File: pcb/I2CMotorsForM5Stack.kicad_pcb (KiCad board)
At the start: 2 copper layers, 60 x 50 mm, 33 parts, among them J1 FFC_connector, J2 2x15socket, J3 Conn_01x06, J4 Conn_01x06, U1 TB6612FNG, U2 ATmega328PB-MU

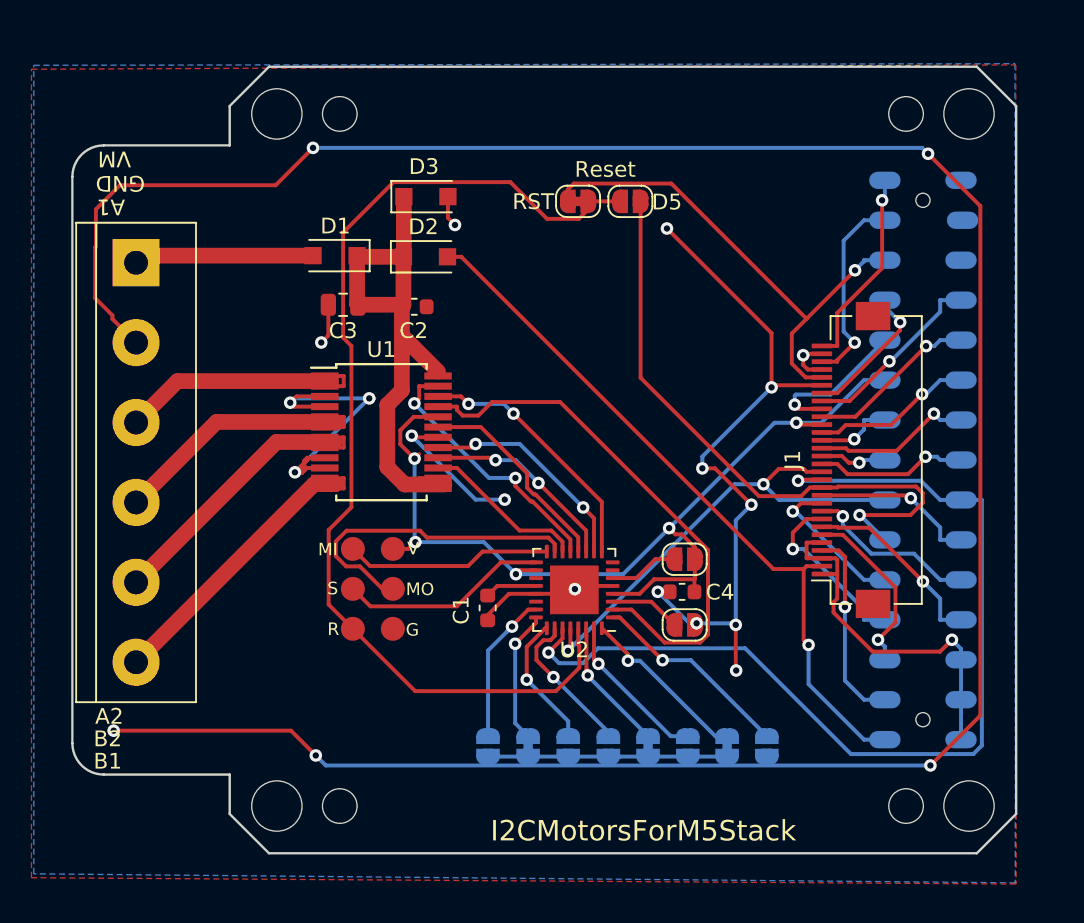
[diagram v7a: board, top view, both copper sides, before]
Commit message: Add connector to support power lines
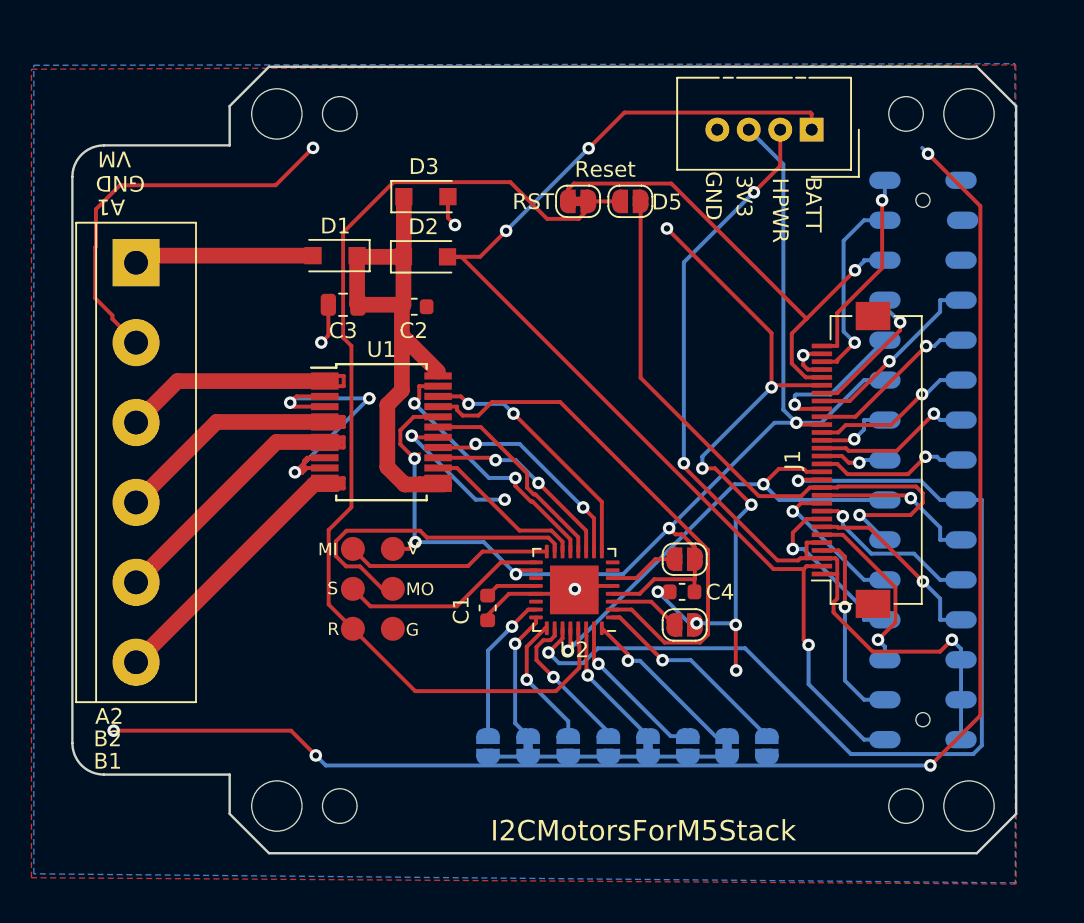
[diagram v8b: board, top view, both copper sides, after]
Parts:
- added J5: Conn_01x04, Connector:NS-Tech_Grove_1x04_P2mm_Vertical, F.Cu at (137.0, 54.0)
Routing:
- net GND: track 267.7 -> 229.0 mm
- net /HPWR: track 23.8 -> 58.1 mm, vias 1 -> 3
- net +BATT: track 45.9 -> 73.9 mm, vias 1 -> 3
- net +3V3: track 62.0 -> 81.9 mm
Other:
- board text added: "3V3"
- board text added: "BATT"
- board text added: "HPWR"
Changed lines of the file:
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@@
   (general
     (thickness 1.6)
-    (drawings 34)
-    (tracks 570)
+    (drawings 38)
+    (tracks 593)
     (zones 0)
-    (modules 33)
+    (modules 34)
     (nets 59)
   )
@@
     (add_net /VM)
     (add_net VCC)
+  )
+  (module Connector:NS-Tech_Grove_1x04_P2mm_Vertical (layer F.Cu)
+    (at 137 54 270)
+    (descr https://statics3.seeedstudio.com/images/opl/datasheet/3470130P1.pdf)
+    (tags Grove-1x04)
+    (fp_text reference J5 (at -1.5 -4 90) (layer F.SilkS) hide
+      (effects (font (size 1 1) (thickness 0.15)))
+    )
+    (fp_text value Conn_01x04 (at 4.19 2.83) (layer F.Fab)
+      (effects (font (size 1 1) (thickness 0.15)))
+    )
+    (fp_line (start -2.9 8.1) (end -2.9 -2.1) (layer F.Fab) (width 0.1))
+    (fp_line (start 2.2 8.1) (end -2.9 8.1) (layer F.Fab) (width 0.1))
+    (fp_line (start 2.2 -2.1) (end 2.2 8.1) (layer F.Fab) (width 0.1))
+    (fp_line (start -2.9 -2.1) (end 2.2 -2.1) (layer F.Fab) (width 0.1))
+    (fp_line (start -3.3 5.9) (end -3.3 8.55) (layer F.SilkS) (width 0.12))
+    (fp_line (start -3.3 -2.5) (end -3.3 0.15) (layer F.SilkS) (width 0.12))
+    (fp_line (start -3.3 8.55) (end 2.55 8.55) (layer F.SilkS) (width 0.12))
+    (fp_line (start -3.3 1.25) (end -3.3 4.75) (layer F.SilkS) (width 0.12))
+    (fp_line (start -3.3 -2.5) (end 2.55 -2.5) (layer F.SilkS) (width 0.12))
+    (fp_line (start 2.55 -2.5) (end 2.55 8.55) (layer F.SilkS) (width 0.12))
+    (fp_line (start -3.3 0.4) (end -3.3 1) (layer F.SilkS) (width 0.12))
+    (fp_line (start -3.3 5) (end -3.3 5.6) (layer F.SilkS) (width 0.12))
+    (fp_line (start -3.45 -2.65) (end 2.7 -2.65) (layer F.CrtYd) (width 0.05))
+    (fp_line (start 2.7 8.7) (end 2.7 -2.65) (layer F.CrtYd) (width 0.05))
+    (fp_line (start -3.45 8.7) (end 2.7 8.7) (layer F.CrtYd) (width 0.05))
+    (fp_line (start -3.45 -2.65) (end -3.45 8.7) (layer F.CrtYd) (width 0.05))
+    (fp_line (start 0 -3) (end 3 -3) (layer F.SilkS) (width 0.12))
+    (fp_line (start 3 -3) (end 3 0) (layer F.SilkS) (width 0.12))
+    (fp_line (start 2.2 -1) (end 0.9 0) (layer F.Fab) (width 0.1))
+    (fp_line (start 0.9 0) (end 2.2 1) (layer F.Fab) (width 0.1))
+    (fp_text user %R (at -2 2) (layer F.Fab)
+      (effects (font (size 1 1) (thickness 0.15)))
+    )
+    (pad 4 thru_hole circle (at 0 6 270) (size 1.524 1.524) (drill 0.762) (layers *.Cu *.Mask)
+      (net 1 GND))
+    (pad 3 thru_hole circle (at 0 4 270) (size 1.524 1.524) (drill 0.762) (layers *.Cu *.Mask)
+      (net 4 +3V3))
+    (pad 2 thru_hole circle (at 0 2 270) (size 1.524 1.524) (drill 0.762) (layers *.Cu *.Mask)
+      (net 26 /HPWR))
+    (pad 1 thru_hole rect (at 0 0 270) (size 1.524 1.524) (drill 0.762) (layers *.Cu *.Mask)
+      (net 2 +BATT))
+    (model ${KISYS3DMOD}/Connector.3dshapes/NS-Tech_Grove_1x04_P2mm_Vertical.wrl
+      (at (xyz 0 0 0))
+      (scale (xyz 0.3937 0.3937 0.3937))
+      (rotate (xyz 0 0 -90))
+    )
   )
   (module Jumper:SolderJumper-2_P1.3mm_Bridged_RoundedPad1.0x1.5mm (layer B.Cu)
@@
     (pad 1 np_thru_hole circle (at 0 0) (size 2.2 2.2) (drill 2.2) (layers *.Cu *.Mask))
   )
+  (gr_text GND (at 130.7488 58.2082 270) (layer F.SilkS)
+    (effects (font (size 1 1) (thickness 0.15)))
+  )
+  (gr_text 3V3 (at 132.6988 58.2332 270) (layer F.SilkS)
+    (effects (font (size 1 1) (thickness 0.15)))
+  )
+  (gr_text HPWR (at 134.9988 59.1332 270) (layer F.SilkS)
+    (effects (font (size 1 1) (thickness 0.15)))
+  )
+  (gr_text BATT (at 137.0988 58.7582 270) (layer F.SilkS)
+    (effects (font (size 1 1) (thickness 0.15)))
+  )
   (gr_text I2CMotorsForM5Stack (at 126.2988 98.5832) (layer F.SilkS)
     (effects (font (size 1.3 1.3) (thickness 0.325)))
@@
   (segment (start 93.0238 57.5332) (end 102.9238 57.5332) (width 0.25) (layer F.Cu) (net 1))
   (segment (start 102.9238 57.5332) (end 105.2988 55.1582) (width 0.25) (layer F.Cu) (net 1))
-  (segment (start 105.2988 55.1582) (end 144.0238 55.1582) (width 0.25) (layer B.Cu) (net 1))
   (via (at 144.3988 55.5332) (size 0.8) (drill 0.4) (layers F.Cu B.Cu) (net 1))
   (segment (start 144.0238 55.1582) (end 144.3988 55.5332) (width 0.25) (layer B.Cu) (net 1))
@@
   (segment (start 137.65 81.75) (end 136.6747 81.75) (width 0.25) (layer F.Cu) (net 2))
   (via (at 136.8026 86.7597) (size 0.8) (layers F.Cu B.Cu) (net 2))
+  (via (at 117.5738 60.4332) (size 0.8) (drill 0.4) (layers F.Cu B.Cu) (net 2))
+  (segment (start 113.849 62.0832) (end 115.9238 62.0832) (width 0.25) (layer F.Cu) (net 2))
+  (segment (start 115.9238 62.0832) (end 117.5738 60.4332) (width 0.25) (layer F.Cu) (net 2))
+  (via (at 122.8238 55.1832) (size 0.8) (drill 0.4) (layers F.Cu B.Cu) (net 2))
+  (segment (start 117.5738 60.4332) (end 122.8238 55.1832) (width 0.25) (layer B.Cu) (net 2))
+  (segment (start 137 52.988) (end 137 54) (width 0.25) (layer F.Cu) (net 2))
+  (segment (start 136.924999 52.912999) (end 137 52.988) (width 0.25) (layer F.Cu) (net 2))
+  (segment (start 125.094001 52.912999) (end 136.924999 52.912999) (width 0.25) (layer F.Cu) (net 2))
+  (segment (start 122.8238 55.1832) (end 125.094001 52.912999) (width 0.25) (layer F.Cu) (net 2))
   (segment (start 141.654 90.24) (end 140.3287 90.24) (width 0.25) (layer B.Cu) (net 3))
   (segment (start 139.1135 84.3526) (end 139.1135 89.0248) (width 0.25) (layer B.Cu) (net 3))
@@
   (segment (start 129.574 80.560608) (end 128.743691 79.730299) (width 0.25) (layer F.Cu) (net 4))
   (segment (start 129.574 81.3082) (end 129.574 80.560608) (width 0.25) (layer F.Cu) (net 4))
+  (segment (start 133.761999 54.761999) (end 133 54) (width 0.25) (layer B.Cu) (net 4))
+  (segment (start 135.198799 56.198799) (end 133.761999 54.761999) (width 0.25) (layer B.Cu) (net 4))
+  (segment (start 135.198799 71.807299) (end 135.198799 56.198799) (width 0.25) (layer B.Cu) (net 4))
+  (segment (start 136.025 72.6335) (end 135.198799 71.807299) (width 0.25) (layer B.Cu) (net 4))
   (segment (start 137.65 67.75) (end 138.6253 67.75) (width 0.25) (layer F.Cu) (net 5))
   (segment (start 141.4778 58.49) (end 141.654 58.3138) (width 0.25) (layer B.Cu) (net 5))
@@
   (segment (start 138.6253 81.3626) (end 138.6253 82.25) (width 0.25) (layer F.Cu) (net 26))
   (segment (start 146.494 90.24) (end 146.494 92.78) (width 0.25) (layer B.Cu) (net 26))
-  (segment (start 137.65 81.25) (end 136.6747 81.25) (width 0.25) (layer F.Cu) (net 26))
   (segment (start 137.65 80.25) (end 136.6747 80.25) (width 0.25) (layer F.Cu) (net 26))
   (segment (start 136.6747 80.25) (end 136.6747 81.25) (width 0.25) (layer F.Cu) (net 26))
@@
   (segment (start 137.65 82.25) (end 138.6253 82.25) (width 0.25) (layer F.Cu) (net 26))
   (via (at 145.9158 86.43) (size 0.8) (layers F.Cu B.Cu) (net 26))
+  (segment (start 137.65 81.25) (end 136.6747 81.25) (width 0.25) (layer F.Cu) (net 26))
+  (segment (start 128.874203 75.431605) (end 128.874203 75.207797) (width 0.25) (layer F.Cu) (net 26))
+  (via (at 128.874203 75.207797) (size 0.8) (drill 0.4) (layers F.Cu B.Cu) (net 26))
+  (segment (start 136.147901 81.386601) (end 134.829199 81.386601) (width 0.25) (layer F.Cu) (net 26))
+  (segment (start 134.829199 81.386601) (end 128.874203 75.431605) (width 0.25) (layer F.Cu) (net 26))
+  (segment (start 136.6747 81.25) (end 136.284502 81.25) (width 0.25) (layer F.Cu) (net 26))
+  (segment (start 136.284502 81.25) (end 136.147901 81.386601) (width 0.25) (layer F.Cu) (net 26))
+  (via (at 133.3238 57.9832) (size 0.8) (drill 0.4) (layers F.Cu B.Cu) (net 26))
+  (segment (start 128.874203 75.207797) (end 128.874203 62.432797) (width 0.25) (layer B.Cu) (net 26))
+  (segment (start 128.874203 62.432797) (end 133.3238 57.9832) (width 0.25) (layer B.Cu) (net 26))
+  (segment (start 135 56.307) (end 135 54) (width 0.25) (layer F.Cu) (net 26))
+  (segment (start 133.3238 57.9832) (end 135 56.307) (width 0.25) (layer F.Cu) (net 26))
   (segment (start 116.399 83.6207) (end 117.0115 83.0082) (width 0.25) (layer F.Cu) (net 27))
   (segment (start 117.0115 83.0082) (end 119.4735 83.0082) (width 0.25) (layer F.Cu) (net 27))
